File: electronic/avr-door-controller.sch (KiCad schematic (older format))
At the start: 65 parts, among them CON1 24V, J1 DOOR1, J2 DOOR2, P1 Digital, P10 DOOR2 BTN, P2 Analog, P3 DOOR1 BTN, P4 RELAY1, P5 RELAY1 CTRL, P6 USB_A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

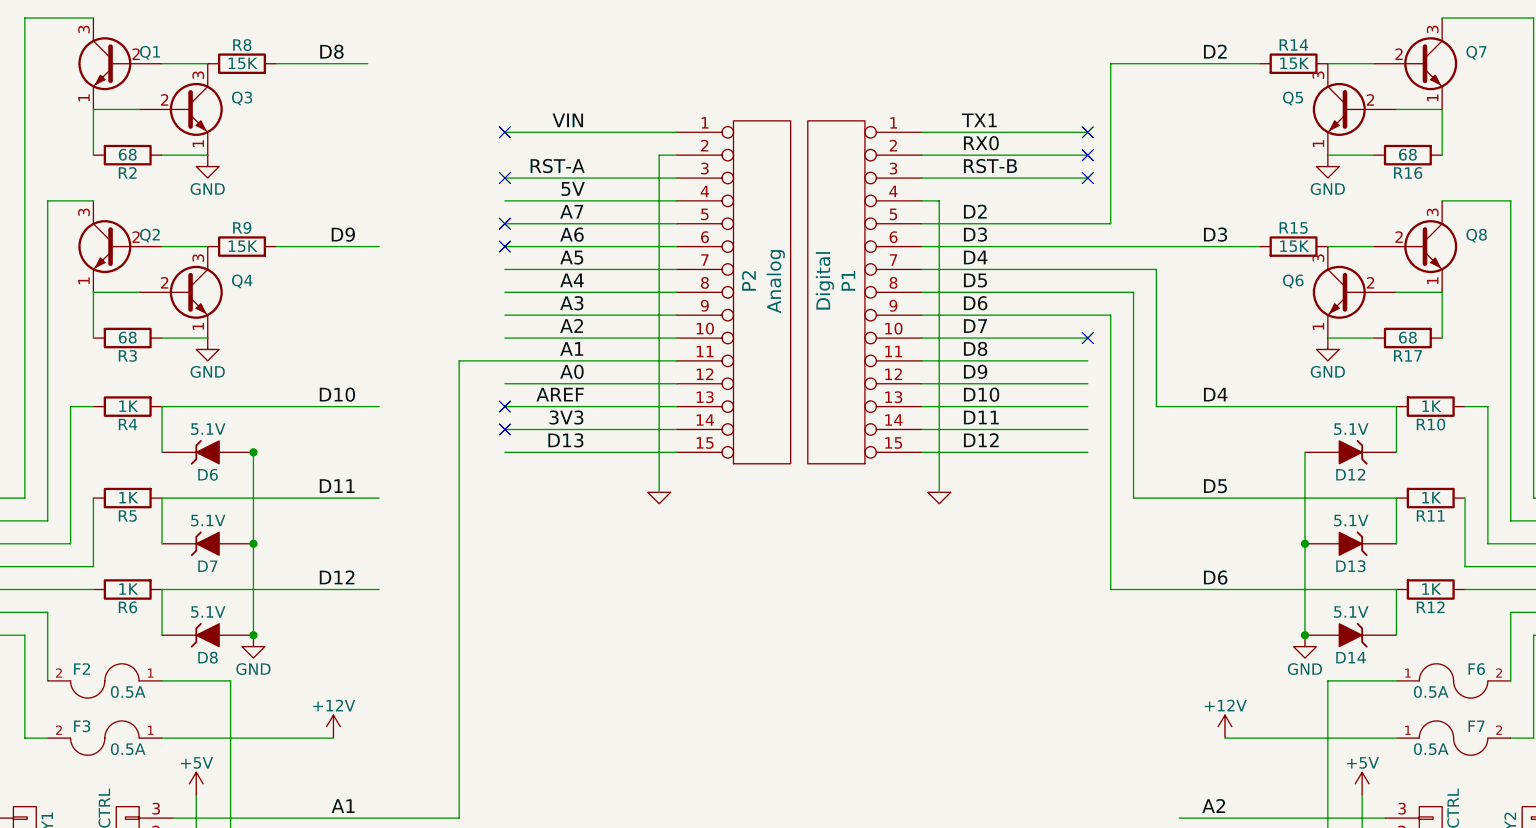
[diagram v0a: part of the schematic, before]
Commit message: electronic: Add pull-down on the wiegand D0 and D1 pins
As the wiegand reader is supposed to pull-up both data lines this
should allow us to detect if the reader is not connected.

Signed-off-by: Alban Bedel <alban.bedel@avionic-design.de>
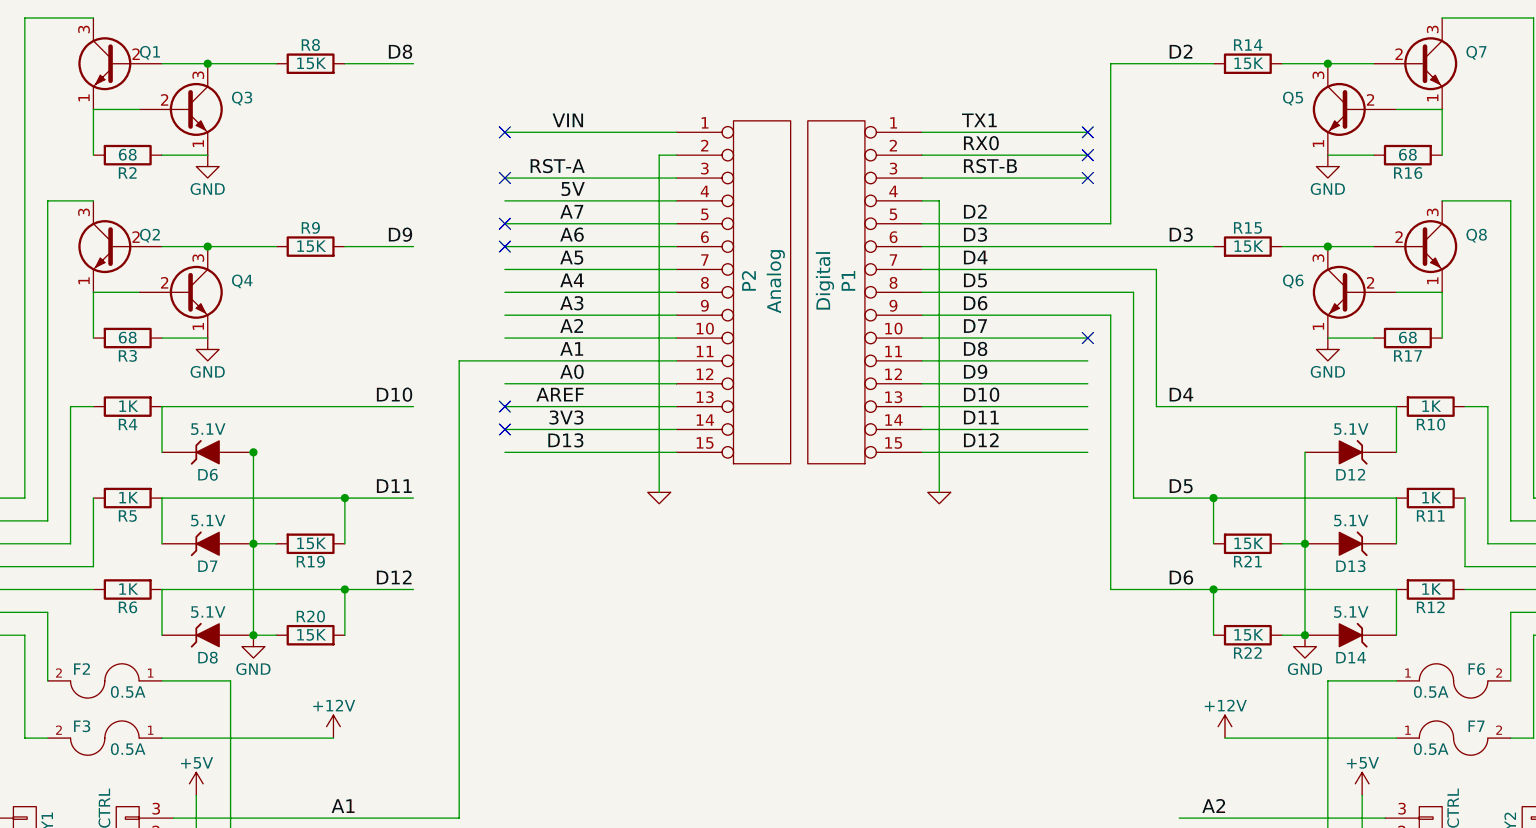
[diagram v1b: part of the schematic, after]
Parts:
- added R19, R20, R21, R22: 15K, Resistors_ThroughHole:Resistor_Horizontal_RM10mm, symbol R
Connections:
- wire segments 178 -> 186
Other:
- moved on the sheet: R14, R15, R8, R9

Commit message: electronic: Fix the missing power input on the +5V regulator
Somehow the power input for the +5V regulator got removed, so the +5V
doesn't run. Add the missing supply and fix the PCB trace.

Signed-off-by: Alban Bedel <albeu@free.fr>
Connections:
- wire segments 186 -> 187

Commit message: electronic: Move the door 1 open button to D7
Pin D13 is connected to the status LED, so that can't be used for the
door 1 open button, use D7 instead.

Signed-off-by: Alban Bedel <albeu@free.fr>
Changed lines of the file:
@@
 NoConn ~ 4700 1800
 NoConn ~ 4700 2600
-NoConn ~ 7250 2300
+NoConn ~ 4700 2800
 NoConn ~ 4700 2700
 $Comp
@@
 $EndComp
 Text Label 1850 1900 2    60   ~ 0
-D13
+D7
 $Comp
 L GND #PWR3

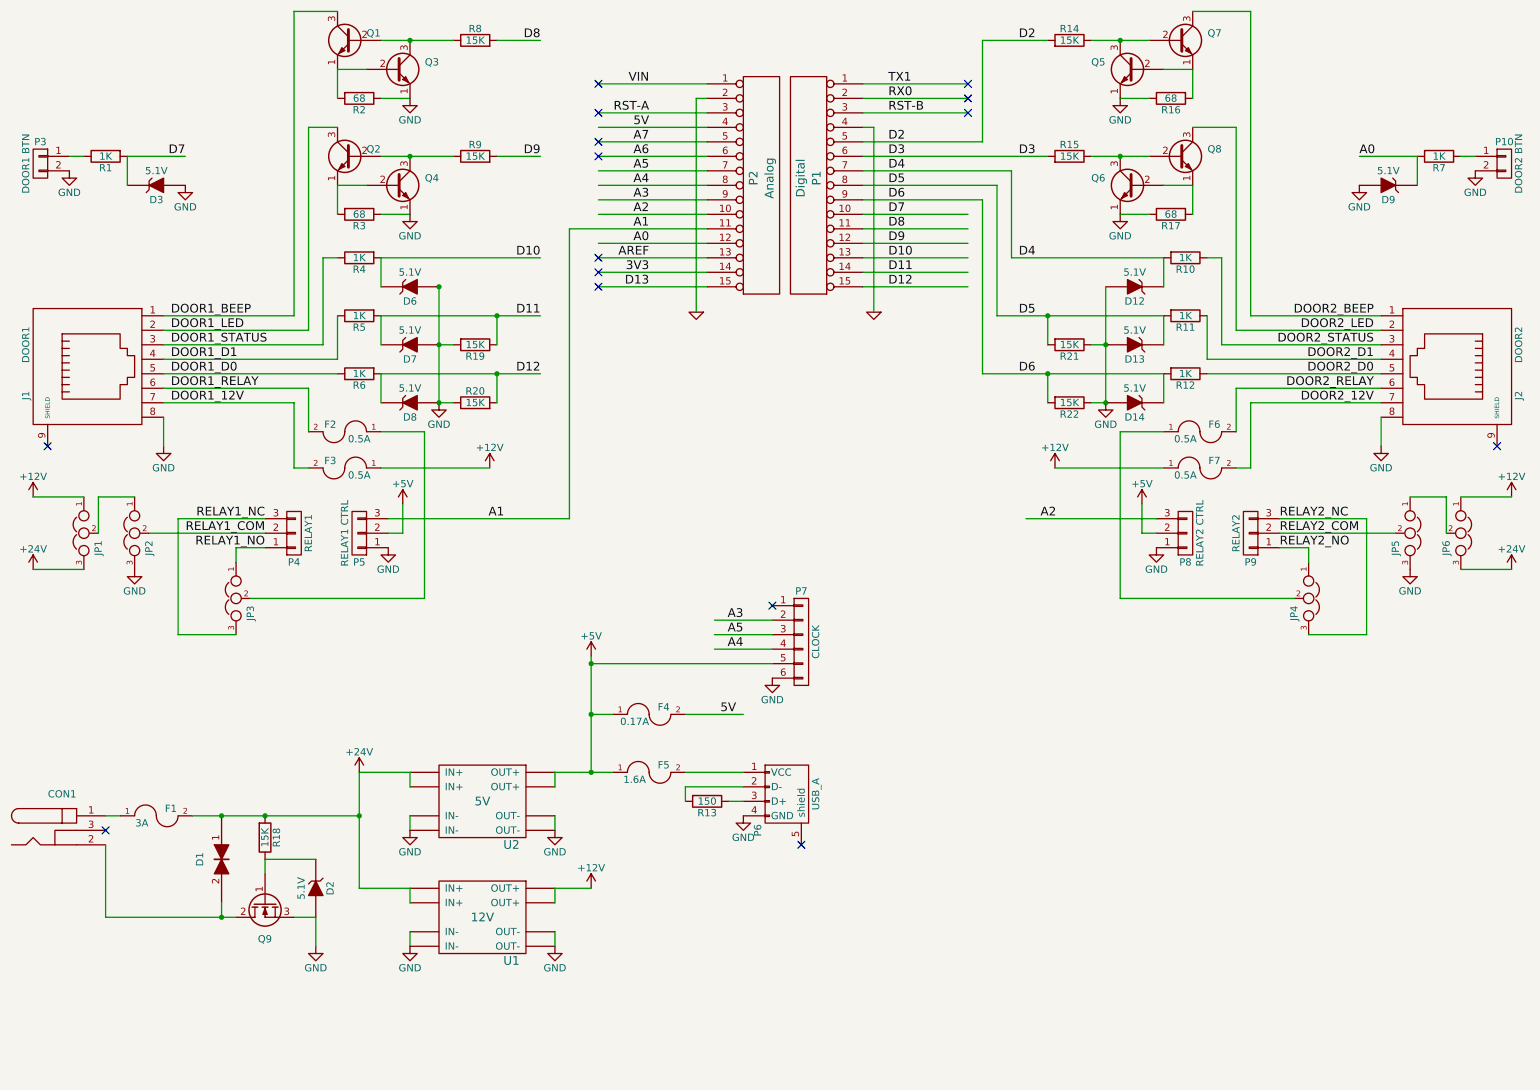
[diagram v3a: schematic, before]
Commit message: electronic: schematics: Integrate the external relay modules
The external relais modules are bulky and annoying in a case, integrate
them on the board.

Signed-off-by: Alban Bedel <albeu@free.fr>
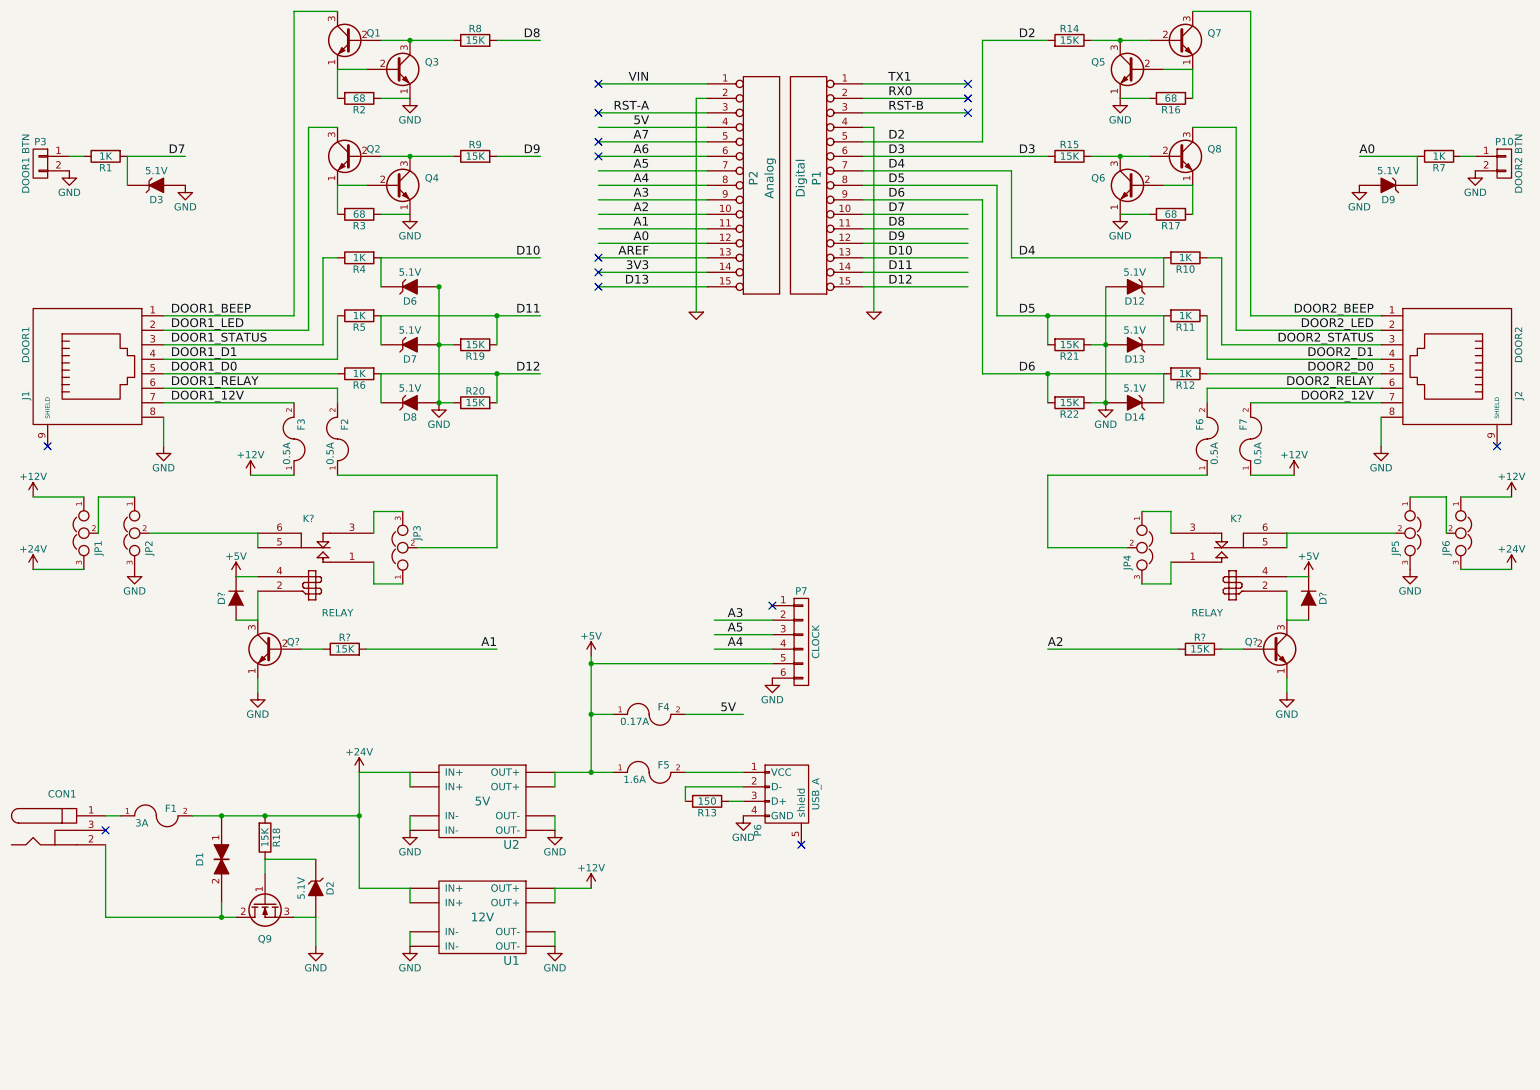
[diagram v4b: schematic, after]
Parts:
- removed P4: RELAY1, Connect:PINHEAD1-3, symbol CONN_01X03
- removed P5: RELAY1 CTRL, Connect:PINHEAD1-3, symbol CONN_01X03
- removed P8: RELAY2 CTRL, Connect:PINHEAD1-3, symbol CONN_01X03
- removed P9: RELAY2, Connect:PINHEAD1-3, symbol CONN_01X03
- added D? (x2): D, symbol D
- added K? (x2): RELAY, symbol RELAY
- added Q? (x2): Q_NPN_EBC, TO_SOT_Packages_THT:TO-92_Inline_Narrow_Oval, symbol Q_NPN_EBC
- added R? (x2): 15K, Resistors_ThroughHole:Resistor_Horizontal_RM10mm, symbol R
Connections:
- net labels removed: RELAY1_COM, RELAY1_NC, RELAY1_NO, RELAY2_COM, RELAY2_NC, RELAY2_NO
- wire segments 187 -> 188
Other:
- moved on the sheet: F2, F3, F6, F7, JP3, JP4

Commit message: electronic: schematics: Allow the board to run from 12V
Add a step up module to allow generating the 24V from 12V instead of
using 24V and a step down for the 12V. We still keep the 12V step down
as we can easily make a PCB that will support both configurations.

Signed-off-by: Alban Bedel <albeu@free.fr>
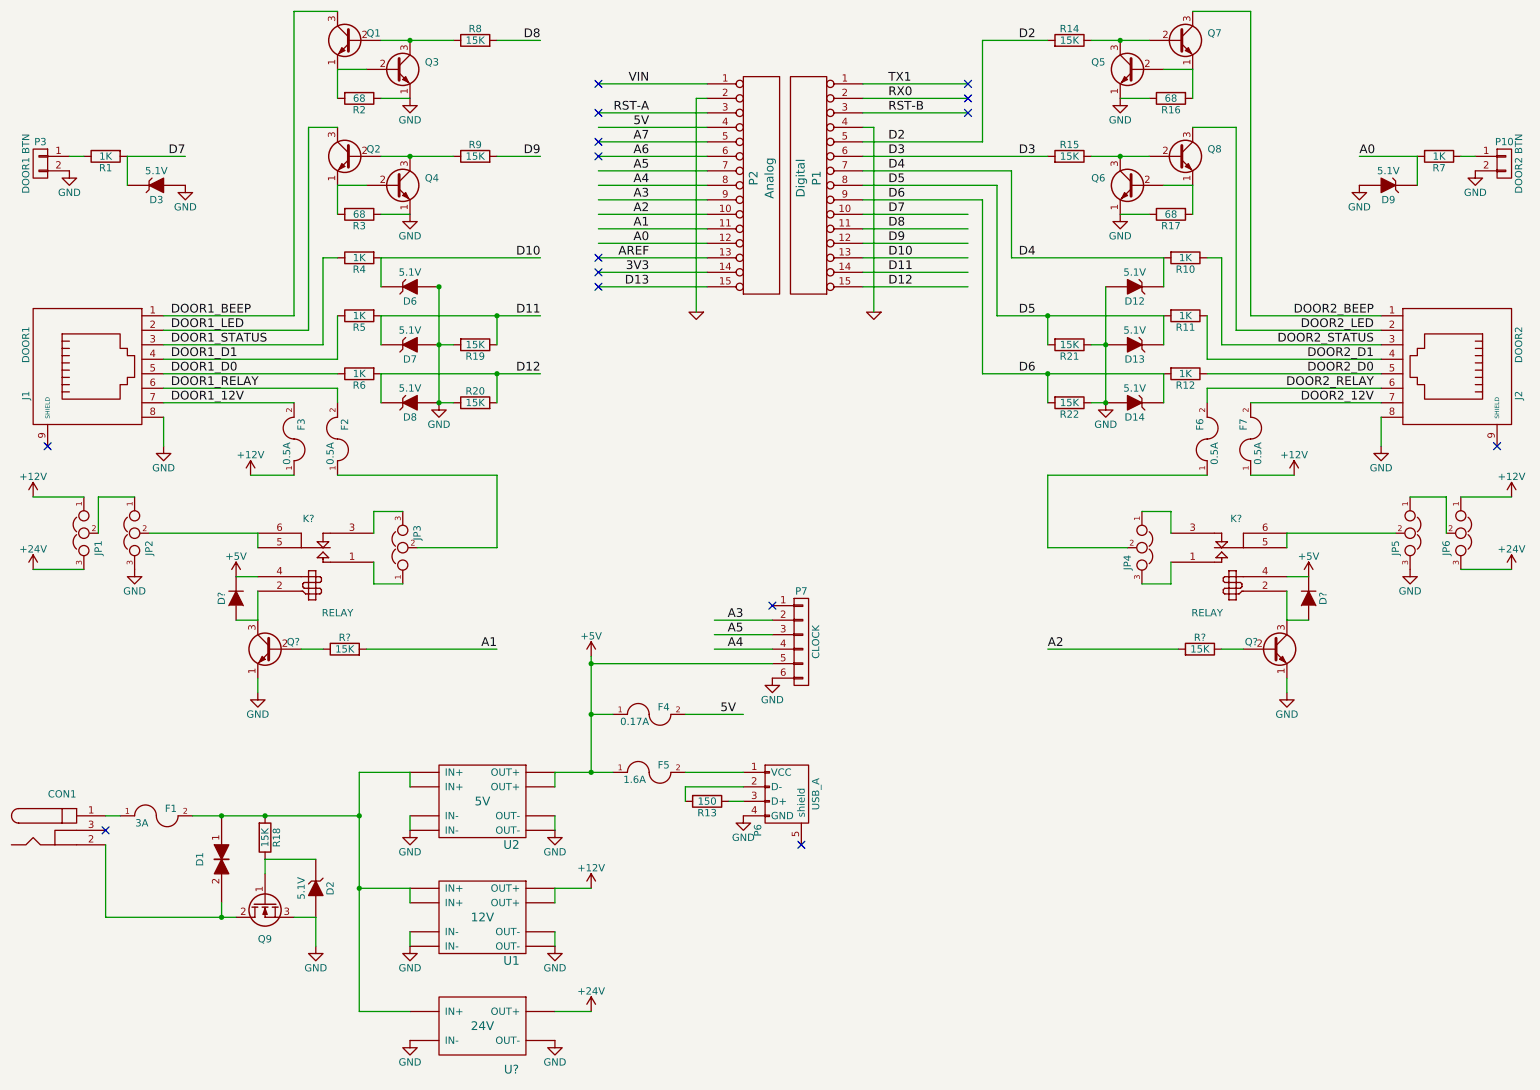
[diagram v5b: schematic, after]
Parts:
- added U?: 24V, symbol MT3608
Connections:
- wire segments 188 -> 210
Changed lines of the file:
@@
-$EndComp
-$Comp
-L +24V #PWR8
-U 1 1 58EE98C7
-P 3050 6150
-F 0 "#PWR8" H 3050 6000 50  0001 C CNN
-F 1 "+24V" H 3050 6290 50  0000 C CNN
-F 2 "" H 3050 6150 50  0000 C CNN
-F 3 "" H 3050 6150 50  0000 C CNN
-	1    3050 6150
-	1    0    0    -1
 $EndComp
 $Comp
@@
 	4400 6950 4650 6950
 Wire Wire Line
-	4400 6150 4800 6150
+	4650 6950 4650 6950
+Wire Wire Line
+	4400 6150 4650 6150
+Wire Wire Line
+	4650 6150 4800 6150
 Wire Wire Line
 	5450 1400 4700 1400
@@
 	3200 3400 3200 3600
 Wire Wire Line
-	3200 3400 4300 3400
+	3200 3400 4000 3400
+Wire Wire Line
+	4000 3400 4300 3400
 Wire Wire Line
 	3200 3000 3200 3200
 Wire Wire Line
-	3200 3000 4300 3000
+	3200 3000 4000 3000
+Wire Wire Line
+	4000 3000 4300 3000
 Wire Wire Line
 	2900 3400 1700 3400
@@
 	8600 3400 8600 3600
 Wire Wire Line
-	7350 3400 8600 3400
+	7350 3400 7800 3400
+Wire Wire Line
+	7800 3400 8600 3400
 Wire Wire Line
 	8600 3000 8600 3200
 Wire Wire Line
-	7450 3000 8600 3000
+	7450 3000 7800 3000
+Wire Wire Line
+	7800 3000 8600 3000
 Wire Wire Line
 	8900 3400 10100 3400
@@
 	7350 2200 7350 3400
 Wire Wire Line
-	3600 2800 3600 3600
-Wire Wire Line
-	4650 5350 4650 6150
+	3600 2800 3600 3200
+Wire Wire Line
+	3600 3200 3600 3600
+Wire Wire Line
+	4650 5350 4650 5400
+Wire Wire Line
+	4650 5400 4650 5750
+Wire Wire Line
+	4650 5750 4650 6150
 Wire Wire Line
 	4650 5750 4800 5750
@@
 	5300 5750 5700 5750
 Wire Wire Line
-	3050 6150 3050 6950
+	3050 6150 3050 6450
+Wire Wire Line
+	3050 6450 3050 6950
 Connection ~ 4650 5750
 Wire Wire Line
@@
 	8800 2100 8800 2300
 Wire Wire Line
-	8100 1900 8500 1900
+	8100 1900 8300 1900
+Wire Wire Line
+	8300 1900 8500 1900
 Wire Wire Line
 	8600 2100 8800 2100
@@
 	8800 1300 8800 1500
 Wire Wire Line
-	8100 1100 8500 1100
+	8100 1100 8300 1100
+Wire Wire Line
+	8300 1100 8500 1100
 Wire Wire Line
 	8600 1300 8800 1300
@@
 	8500 1500 8300 1500
 Wire Wire Line
-	8200 2800 8200 3600
+	8200 2800 8200 3200
+Wire Wire Line
+	8200 3200 8200 3600
 Wire Wire Line
 	7350 1800 7350 1100
@@
 	2900 2100 2900 2300
 Wire Wire Line
-	3200 1900 3700 1900
+	3200 1900 3400 1900
+Wire Wire Line
+	3400 1900 3700 1900
 Wire Wire Line
 	3100 2100 2900 2100
@@
 	2900 1300 2900 1500
 Wire Wire Line
-	3200 1100 3700 1100
+	3200 1100 3400 1100
+Wire Wire Line
+	3400 1100 3700 1100
 Wire Wire Line
 	3100 1300 2900 1300
@@
 	2400 6750 2400 6850
 Wire Wire Line
-	1300 7150 2200 7150
-Wire Wire Line
-	1900 6450 3050 6450
+	1300 7150 2100 7150
+Wire Wire Line
+	2100 7150 2200 7150
+Wire Wire Line
+	1900 6450 2100 6450
+Wire Wire Line
+	2100 6450 2400 6450
+Wire Wire Line
+	2400 6450 3050 6450
 Connection ~ 2400 6450
 Wire Wire Line
@@
 Wire Wire Line
 	7800 4100 7800 4600
+$Comp
+L MT3608 U?
+U 1 1 59BF6CF4
+P 3900 7900
+F 0 "U?" H 4100 8200 60  0000 C CNN
+F 1 "24V" H 3900 7900 60  0000 C CNN
+F 2 "" H 3900 7900 60  0000 C CNN
+F 3 "" H 3900 7900 60  0000 C CNN
+	1    3900 7900
+	1    0    0    1
+$EndComp
+$Comp
+L +24V #PWR?
+U 1 1 59BF6F6A
+P 4650 7800
+F 0 "#PWR?" H 4650 7650 50  0001 C CNN
+F 1 "+24V" H 4650 7940 50  0000 C CNN
+F 2 "" H 4650 7800 50  0000 C CNN
+F 3 "" H 4650 7800 50  0000 C CNN
+	1    4650 7800
+	1    0    0    -1
+$EndComp
+Wire Wire Line
+	4400 7800 4650 7800
+Wire Wire Line
+	4650 7800 4650 7800
+$Comp
+L GND #PWR?
+U 1 1 59BF724D
+P 4400 8000
+F 0 "#PWR?" H 4400 7750 50  0001 C CNN
+F 1 "GND" H 4400 7850 50  0000 C CNN
+F 2 "" H 4400 8000 50  0000 C CNN
+F 3 "" H 4400 8000 50  0000 C CNN
+	1    4400 8000
+	1    0    0    -1
+$EndComp
+$Comp
+L GND #PWR?
+U 1 1 59BF7F5A
+P 3400 8000
+F 0 "#PWR?" H 3400 7750 50  0001 C CNN
+F 1 "GND" H 3400 7850 50  0000 C CNN
+F 2 "" H 3400 8000 50  0000 C CNN
+F 3 "" H 3400 8000 50  0000 C CNN
+	1    3400 8000
+	1    0    0    -1
+$EndComp
+Wire Wire Line
+	3050 7800 3400 7800
+Connection ~ 3050 6950
+Wire Wire Line
+	3050 6950 3050 7800
 $EndSCHEMATC
